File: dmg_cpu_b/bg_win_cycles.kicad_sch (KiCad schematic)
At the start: 96 parts

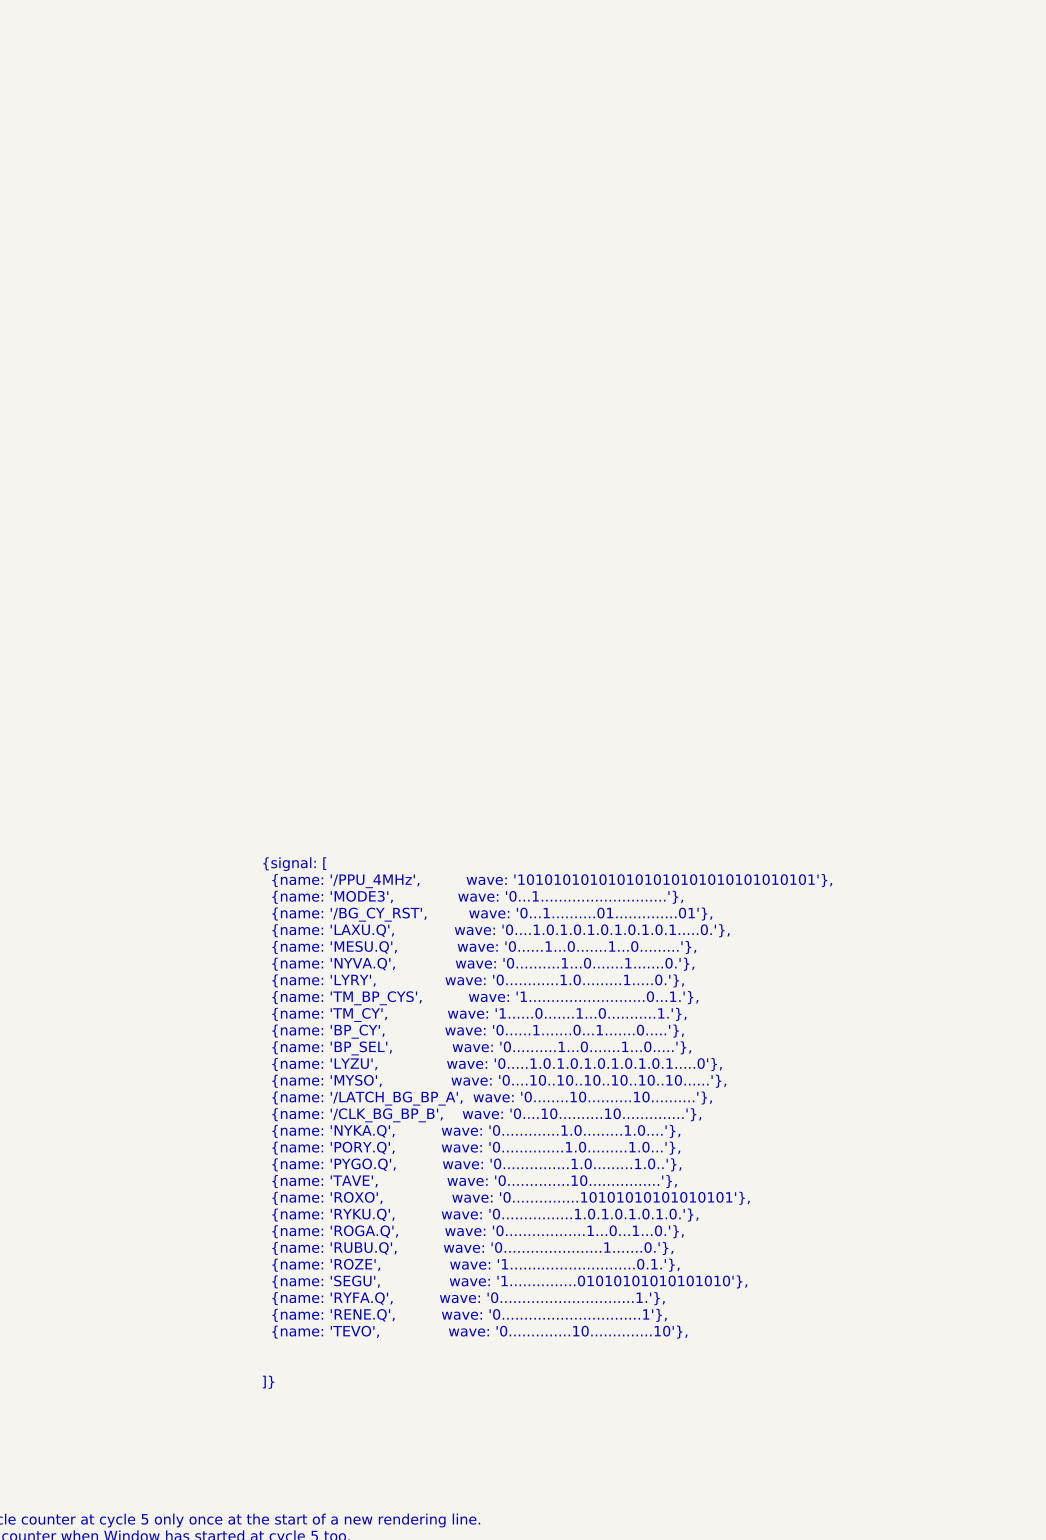
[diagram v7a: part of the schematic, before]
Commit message: Fixed DMA phi2 signal. Notes tidied up, page order modified and draft pdf created for review.
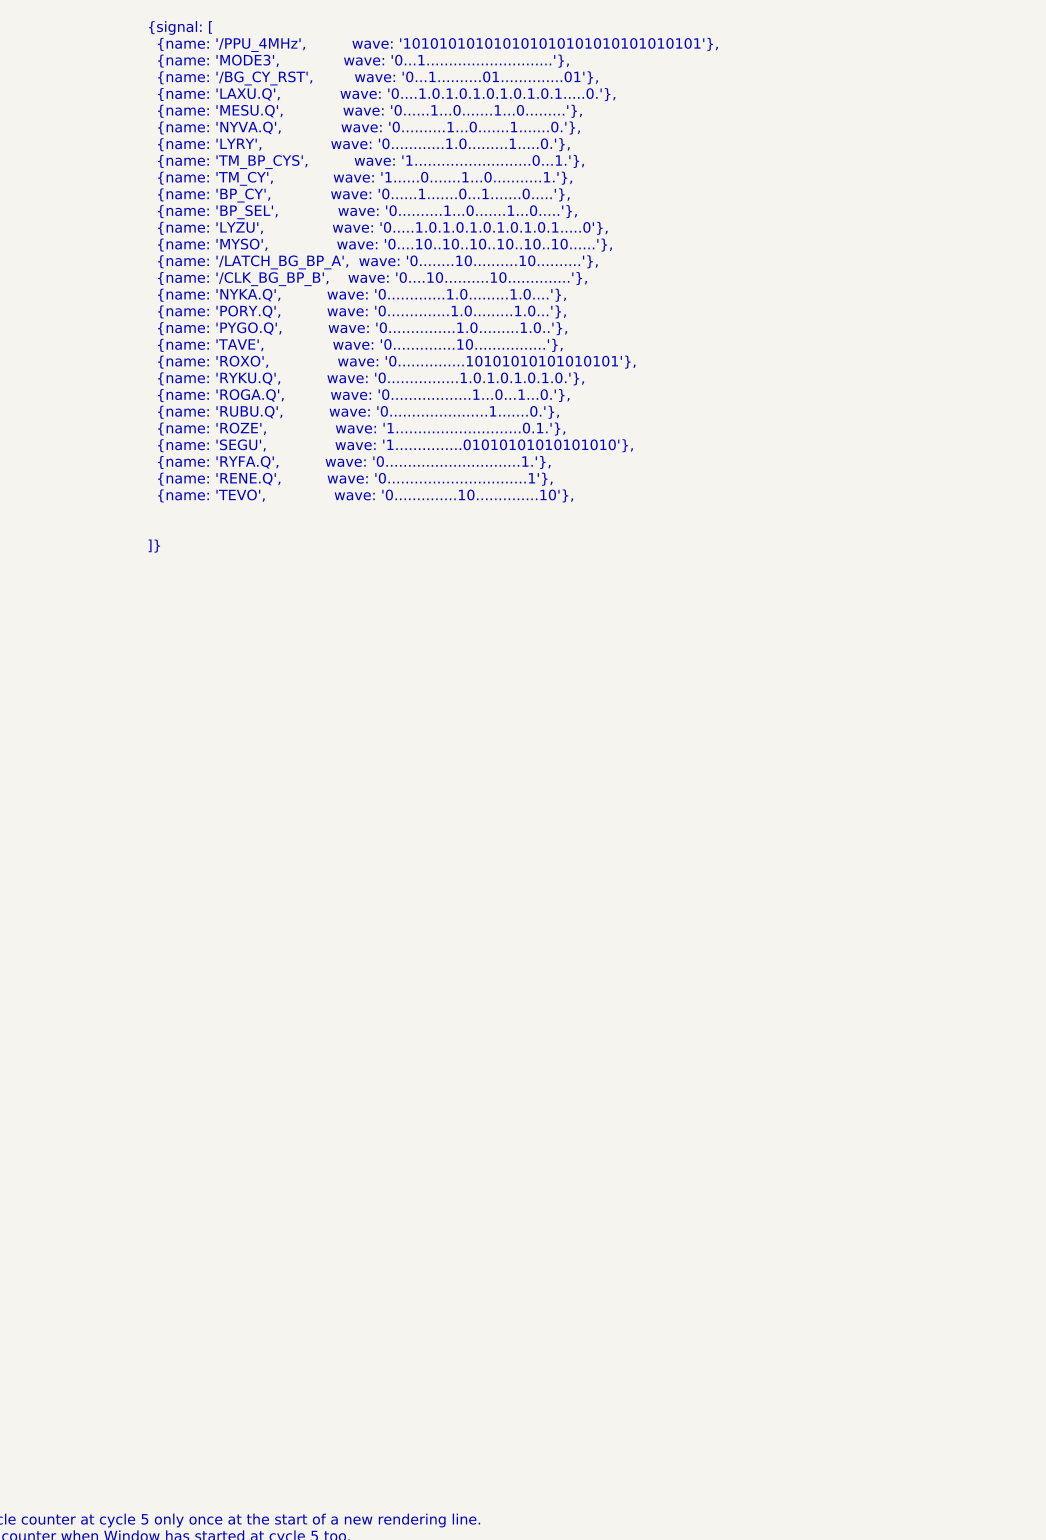
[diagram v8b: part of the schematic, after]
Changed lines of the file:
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@@
   (title_block
     (title "DMG CPU B")
-    (date "2022-05-19")
-    (rev "0")
+    (date "2022-07-08")
+    (rev "0.1")
     (company "CC-BY-SA-4.0 Régis Galland & Michael Singer -- Derived work from Furrtek")
     (comment 1 "https://github.com/msinger/dmg-schematics")
@@
   )
   (text "{signal: [\n  {name: '/PPU_4MHz',  		wave: '101010101010101010101010101010101'},\n  {name: 'MODE3',      		wave: '0...1............................'},\n  {name: '/BG_CY_RST', 		wave: '0...1..........01..............01'},\n  {name: 'LAXU.Q',     		wave: '0....1.0.1.0.1.0.1.0.1.0.1.....0.'},\n  {name: 'MESU.Q',     		wave: '0......1...0.......1...0.........'},\n  {name: 'NYVA.Q',     		wave: '0..........1...0.......1.......0.'},\n  {name: 'LYRY',       		wave: '0............1.0.........1.....0.'},\n  {name: 'TM_BP_CYS',  		wave: '1..........................0...1.'},\n  {name: 'TM_CY',     		wave: '1......0.......1...0...........1.'},\n  {name: 'BP_CY',     		wave: '0......1.......0...1.......0.....'},\n  {name: 'BP_SEL',     		wave: '0..........1...0.......1...0.....'},\n  {name: 'LYZU',       		wave: '0.....1.0.1.0.1.0.1.0.1.0.1.....0'},\n  {name: 'MYSO',       		wave: '0....10..10..10..10..10..10......'},\n  {name: '/LATCH_BG_BP_A',  wave: '0........10..........10..........'},\n  {name: '/CLK_BG_BP_B',    wave: '0....10..........10..............'},\n  {name: 'NYKA.Q',          wave: '0.............1.0.........1.0....'},\n  {name: 'PORY.Q',          wave: '0..............1.0.........1.0...'},\n  {name: 'PYGO.Q',          wave: '0...............1.0.........1.0..'},\n  {name: 'TAVE',       		wave: '0..............10................'},\n  {name: 'ROXO',       		wave: '0...............10101010101010101'},\n  {name: 'RYKU.Q',          wave: '0................1.0.1.0.1.0.1.0.'},\n  {name: 'ROGA.Q',          wave: '0..................1...0...1...0.'},\n  {name: 'RUBU.Q',          wave: '0......................1.......0.'},\n  {name: 'ROZE',       		wave: '1............................0.1.'},\n  {name: 'SEGU',       		wave: '1...............01010101010101010'},\n  {name: 'RYFA.Q',          wave: '0..............................1.'},\n  {name: 'RENE.Q',          wave: '0...............................1'},  \n  {name: 'TEVO',       		wave: '0..............10..............10'},\n   \n  \n]}"
-    (at 312.42 93.98 0)
+    (at 298.45 -8.255 0)
     (effects (font (size 1.27 1.27)) (justify left bottom))
   )
